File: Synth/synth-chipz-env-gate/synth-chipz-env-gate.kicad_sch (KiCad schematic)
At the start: 21 parts, among them Q1 BC860W, U1 TL074

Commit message: Change recommended pot part values from 10K to 1M.
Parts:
- C4: value 1uF -> 2.2uF
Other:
- note added: "1M"
- note removed: "10K"
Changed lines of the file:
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@@
 		(comment 1 "Based upon a Moog EG")
 	)
-	(text "10K"
+	(text "1M"
 		(exclude_from_sim no)
 		(at 109.1771 101.5379 0)
@@
 		)
 	)
-	(text "10K"
+	(text "1M"
 		(exclude_from_sim no)
 		(at 149.8171 101.5379 0)
@@
 		(dnp no)
 		(property "Reference" "C4"
-			(at 157.48 83.82 0)
+			(at 160.02 83.82 0)
 			(do_not_autoplace yes)
 			(effects
@@
 					(bold yes)
 				)
-				(justify left)
-			)
-		)
-		(property "Value" "1uF"
-			(at 157.4813 86.5375 0)
+				(justify right)
+			)
+		)
+		(property "Value" "2.2uF"
+			(at 160.02 86.36 0)
 			(do_not_autoplace yes)
 			(effects
@@
 					(size 1 1)
 				)
-				(justify left)
-			)
-		)
+				(justify right)
+			)
+		)

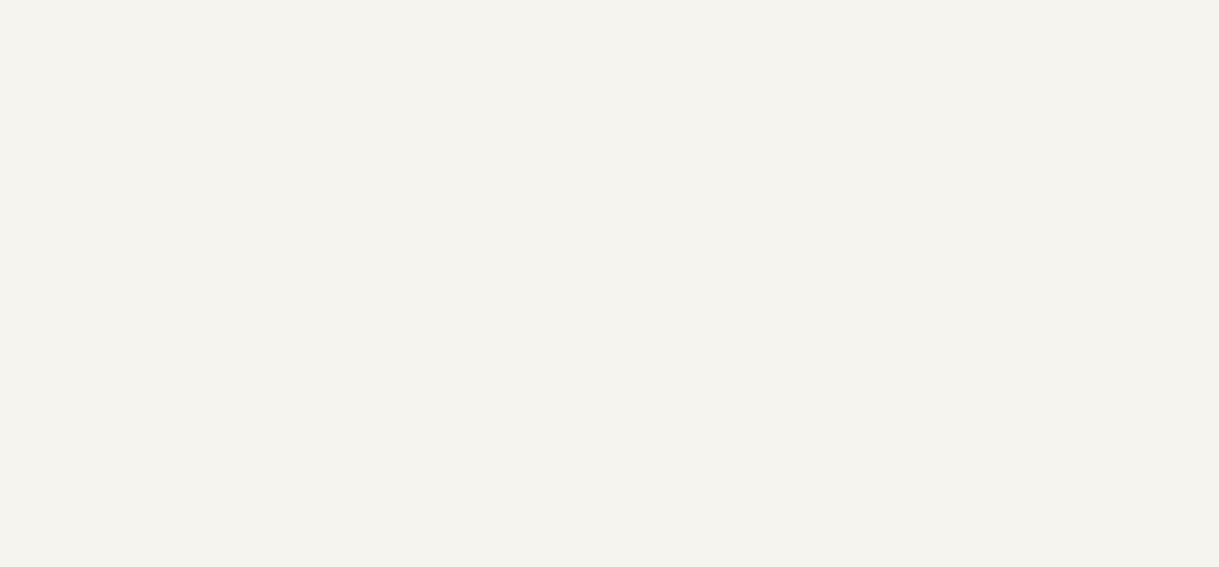
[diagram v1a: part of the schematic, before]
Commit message: Add note regarding faceplate mounts. Bumped Rev. to B.
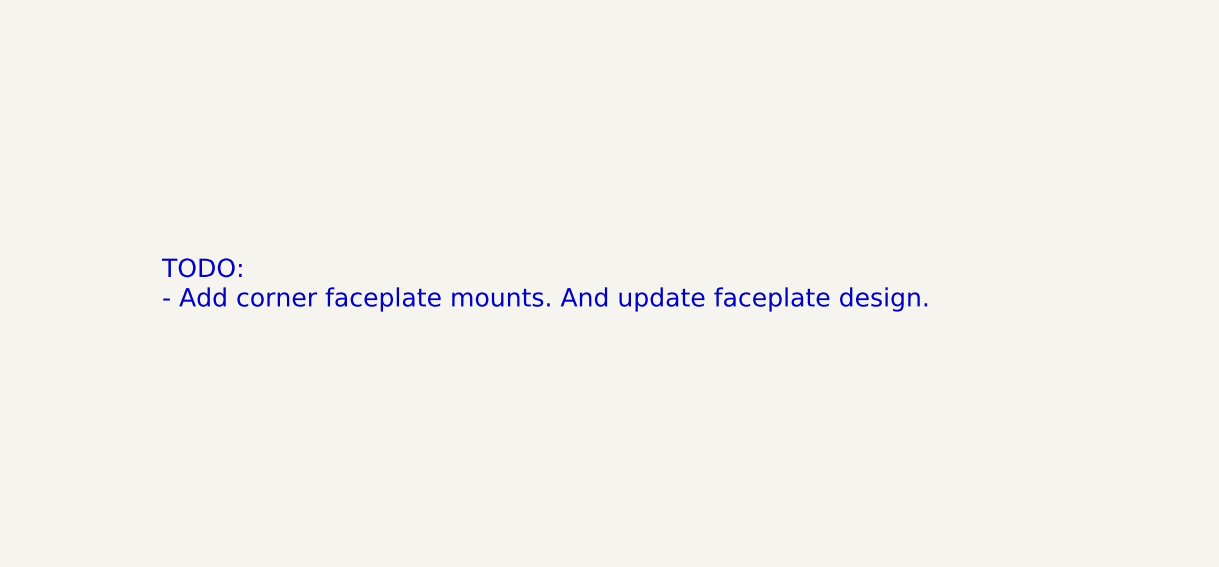
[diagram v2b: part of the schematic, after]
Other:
- note added: "TODO: - Add corner faceplate mounts. And update faceplate design."
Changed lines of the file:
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@@
 	(title_block
 		(title "CHIPz - Envelope Gate")
-		(date "2025-11-04")
-		(rev "A")
+		(date "2025-11-22")
+		(rev "B")
 		(company "Circuit Monkey")
 		(comment 1 "Based upon a Moog EG")
 	)
+	(text "TODO:\n- Add corner faceplate mounts. And update faceplate design.\n"
+		(exclude_from_sim no)
+		(at 177.8 162.56 0)
+		(effects
+			(font
+				(size 2.032 2.032)
+			)
+			(justify left bottom)
+		)
+	)
 	(text "1M"
